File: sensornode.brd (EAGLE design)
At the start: 113 x 59.7 mm, 72 parts, among them IC1 CP2104, Q1 mmbt2222, Q2 mmbt2222, Q3 DMG3415U, SW2 KMR2, U1 TSL2591, U2 AP2112-3.3, U3 MCP73831T-2ACI/OT, U4 BMEx80, X2 ESP32_WROOM32_SKINNY, X4 20329

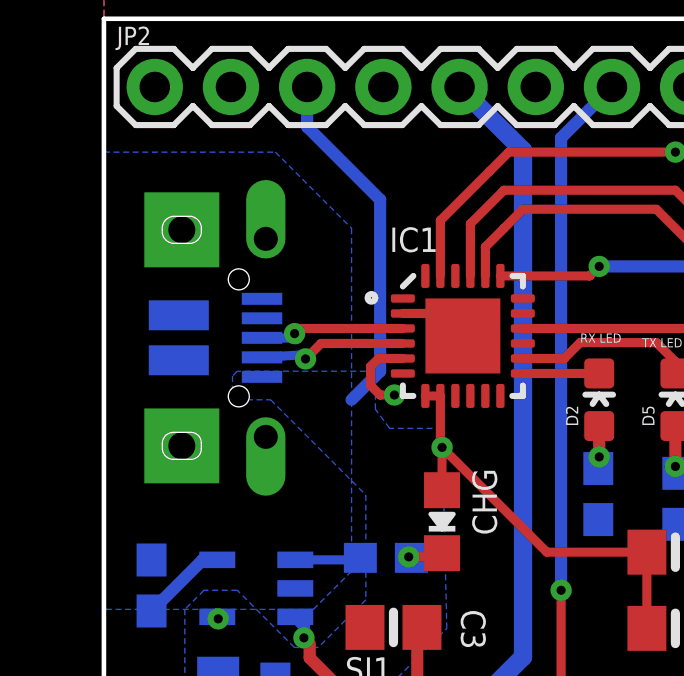
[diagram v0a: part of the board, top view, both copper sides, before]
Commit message: USB: Swapping the USB part out - twas unobtanium
the 4UCONN connector that Adafruit used is basically made of unobtanium
and more or less doesn't exist.  The part that was trying to be used
the rear prongs did not match up by any stretch of the imagination.

A mess of e-mails an annoyance ensued.

I'm swapping out the part on everything I can now, this seems to be
more common, and there's parts that are similar enough to it that
replacing it won't be a big deal.  New part is the
Amphenol FCI 10118193-0001LF
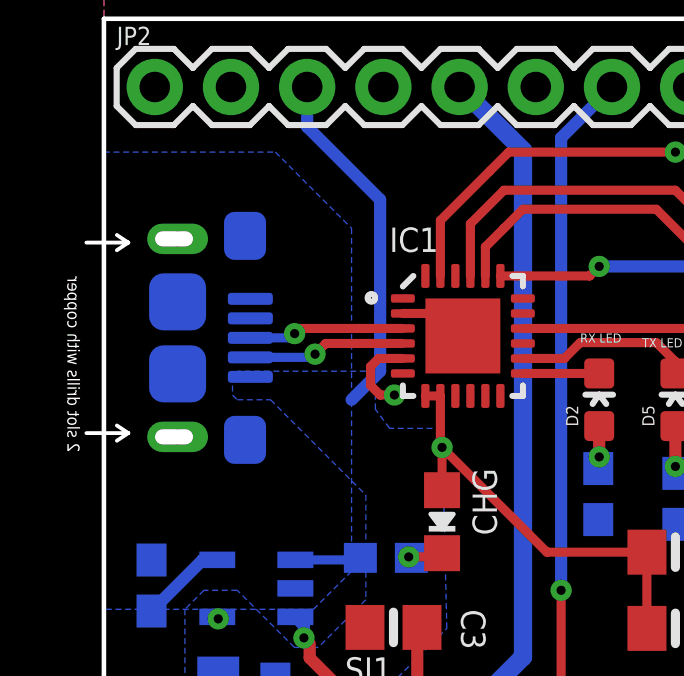
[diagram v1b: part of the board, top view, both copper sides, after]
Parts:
- X4: device microbuilder:4UCONN_20329_V2 -> microbuilder:MICRO-USB5+6P-SMD-0.65-B
- moved X4 0.63 mm to (5.13, 49.1)
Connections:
- net GND: now also X4.5, X4.S1, X4.S2, X4.S3, X4.S4, X4.S5, X4.S6; no longer X4.BASE@1, X4.BASE@2, X4.GND, X4.SPRT@1, X4.SPRT@2, X4.SPRT@3, X4.SPRT@4
- net USBD_N: now also X4.2; no longer X4.D-
- net USBD_P: now also X4.3; no longer X4.D+
- net VBUS: now also X4.1; no longer X4.VBUS
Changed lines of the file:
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@@
 <layer number="115" name="ReferenceISLANDS" color="7" fill="1" visible="yes" active="yes"/>
 <layer number="116" name="Patch_BOT" color="9" fill="4" visible="yes" active="yes"/>
+<layer number="117" name="BACKMAAT1" color="7" fill="1" visible="no" active="no"/>
 <layer number="118" name="Rect_Pads" color="7" fill="1" visible="yes" active="yes"/>
+<layer number="119" name="KAP_TEKEN" color="7" fill="1" visible="no" active="no"/>
+<layer number="120" name="KAP_MAAT1" color="7" fill="1" visible="no" active="no"/>
 <layer number="121" name="_tsilk" color="7" fill="1" visible="yes" active="yes"/>
 <layer number="122" name="_bsilk" color="7" fill="1" visible="yes" active="yes"/>
@@
 <layer number="128" name="_bValues" color="7" fill="1" visible="yes" active="yes"/>
 <layer number="129" name="Mask" color="7" fill="1" visible="yes" active="yes"/>
+<layer number="130" name="SMDSTROOK" color="7" fill="1" visible="no" active="no"/>
 <layer number="131" name="tAdjust" color="7" fill="1" visible="yes" active="yes"/>
 <layer number="132" name="bAdjust" color="7" fill="1" visible="yes" active="yes"/>
+<layer number="133" name="bottom_silk" color="7" fill="1" visible="no" active="no"/>
 <layer number="144" name="Drill_legend" color="7" fill="1" visible="yes" active="yes"/>
 <layer number="145" name="DrillLegend_01-16" color="2" fill="9" visible="yes" active="yes"/>
@@
 <attribute name="NAME" x="4.137" y="43.33875" size="0.8128" layer="26" ratio="18" rot="MR180"/>
 </element>
-<element name="X4" library="microbuilder" package="4UCONN_20329_V2" value="20329" x="4.4958" y="49.05375" rot="MR90"/>
+<element name="X4" library="microbuilder" package="MICRO-USB5+6P-SMD-0.65-B" value="20329" x="5.1308" y="49.05375" rot="MR90"/>
 <element name="JP2" library="SparkFun-Connectors" package="1X29" value="" x="1.695" y="57.41625"/>
 <element name="Q1" library="SparkFun" package="SOT23-3" value="mmbt2222" x="93.0275" y="57.15" rot="R180"/>
@@
 <contactref element="SW2" pad="A"/>
 <contactref element="SW2" pad="A'"/>
-<contactref element="X4" pad="BASE@1"/>
-<contactref element="X4" pad="BASE@2"/>
-<contactref element="X4" pad="GND"/>
-<contactref element="X4" pad="SPRT@1"/>
-<contactref element="X4" pad="SPRT@2"/>
-<contactref element="X4" pad="SPRT@3"/>
-<contactref element="X4" pad="SPRT@4"/>
+<contactref element="X4" pad="5"/>
 <contactref element="IC1" pad="2"/>
 <contactref element="IC1" pad="THERM"/>
@@
 <contactref element="C21" pad="2"/>
 <contactref element="C20" pad="2"/>
+<contactref element="X4" pad="S1"/>
+<contactref element="X4" pad="S2"/>
+<contactref element="X4" pad="S3"/>
+<contactref element="X4" pad="S4"/>
+<contactref element="X4" pad="S5"/>
+<contactref element="X4" pad="S6"/>
 <wire x1="96.995" y1="44.4275" x2="94.615" y2="43.18" width="0" layer="19" extent="1-1"/>
 </signal>
@@
 <wire x1="9.09625" y1="33.44875" x2="7.3025" y2="35.2425" width="0.4064" layer="16"/>
 <wire x1="7.3025" y1="35.2425" x2="7.3025" y2="37.465" width="0.4064" layer="16"/>
-<contactref element="X4" pad="VBUS"/>
+<contactref element="X4" pad="1"/>
 <contactref element="IC1" pad="8"/>
 <contactref element="C20" pad="1"/>
@@
 </signal>
 <signal name="USBD_P" class="1">
-<contactref element="X4" pad="D+"/>
+<contactref element="X4" pad="3"/>
 <contactref element="IC1" pad="3"/>
-<wire x1="5.2708" y1="49.05375" x2="6.419565625" y2="49.042203125" width="0.3048" layer="16"/>
 <via x="6.357075" y="49.195234375" extent="1-16" drill="0.3048"/>
-<wire x1="6.419565625" y1="49.042203125" x2="6.357075" y2="49.195234375" width="0.4064" layer="16"/>
 <wire x1="9.96484375" y1="49.367246875" x2="6.5290875" y2="49.367246875" width="0.3048" layer="1"/>
 <wire x1="6.5290875" y1="49.367246875" x2="6.357075" y2="49.195234375" width="0.3048" layer="1"/>
+<wire x1="4.8808" y1="49.05375" x2="6.215590625" y2="49.05375" width="0.3048" layer="16"/>
+<wire x1="6.215590625" y1="49.05375" x2="6.357075" y2="49.195234375" width="0.3048" layer="16"/>
 </signal>
 <signal name="USBD_N" class="1">
-<contactref element="X4" pad="D-"/>
+<contactref element="X4" pad="2"/>
 <contactref element="IC1" pad="4"/>
-<wire x1="5.2708" y1="48.40375" x2="6.65755625" y2="48.48991875" width="0.3048" layer="16"/>
-<via x="6.720215625" y="48.35099375" extent="1-16" drill="0.3048"/>
-<wire x1="6.65755625" y1="48.48991875" x2="6.720215625" y2="48.35099375" width="0.4064" layer="16"/>
-<wire x1="9.96484375" y1="48.867246875" x2="7.23646875" y2="48.867246875" width="0.3048" layer="1"/>
-<wire x1="7.23646875" y1="48.867246875" x2="6.720215625" y2="48.35099375" width="0.3048" layer="1"/>
+<via x="7.037715625" y="48.50974375" extent="1-16" drill="0.3048"/>
+<wire x1="4.8808" y1="48.40375" x2="6.931721875" y2="48.40375" width="0.3048" layer="16"/>
+<wire x1="6.931721875" y1="48.40375" x2="7.037715625" y2="48.50974375" width="0.3048" layer="16"/>
+<wire x1="9.96484375" y1="48.867246875" x2="7.39521875" y2="48.867246875" width="0.3048" layer="1"/>
+<wire x1="7.39521875" y1="48.867246875" x2="7.037715625" y2="48.50974375" width="0.3048" layer="1"/>
 </signal>
 <signal name="RTS">

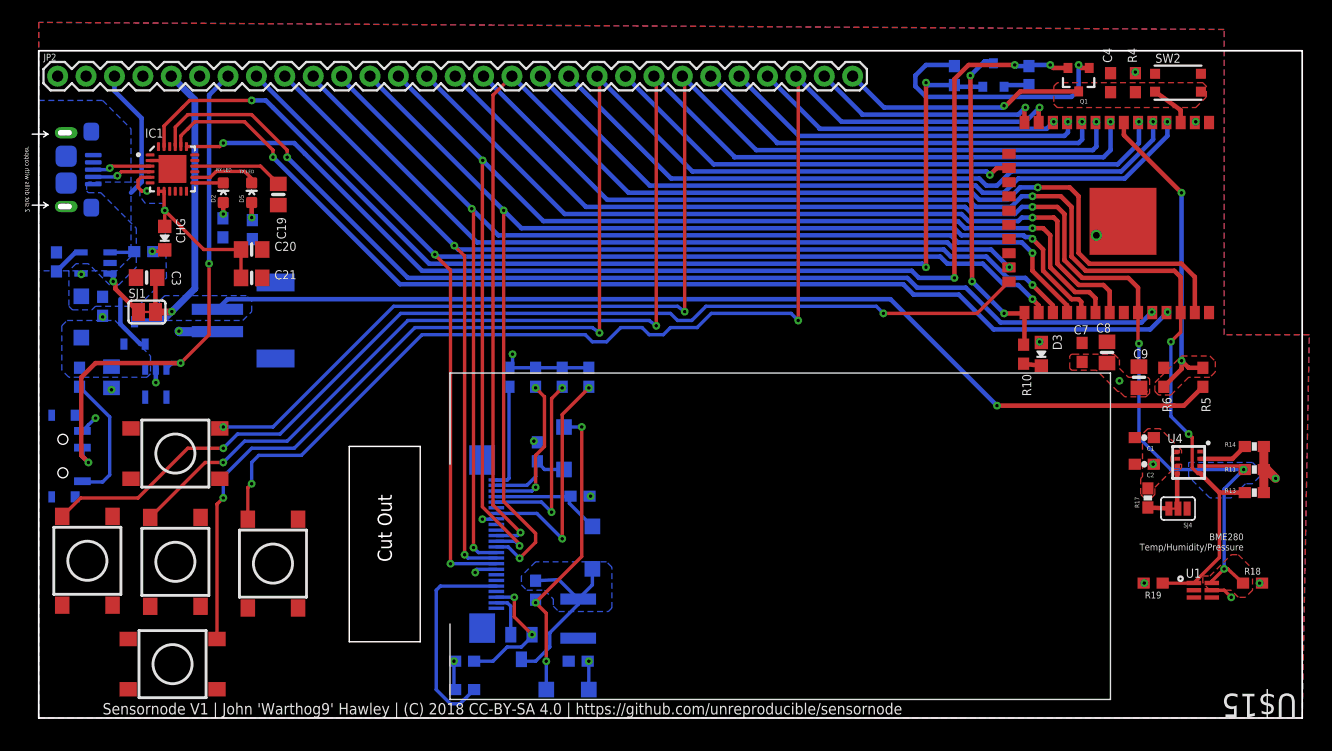
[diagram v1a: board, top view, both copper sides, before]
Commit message: Moving sensors down-making room for wifi keep out
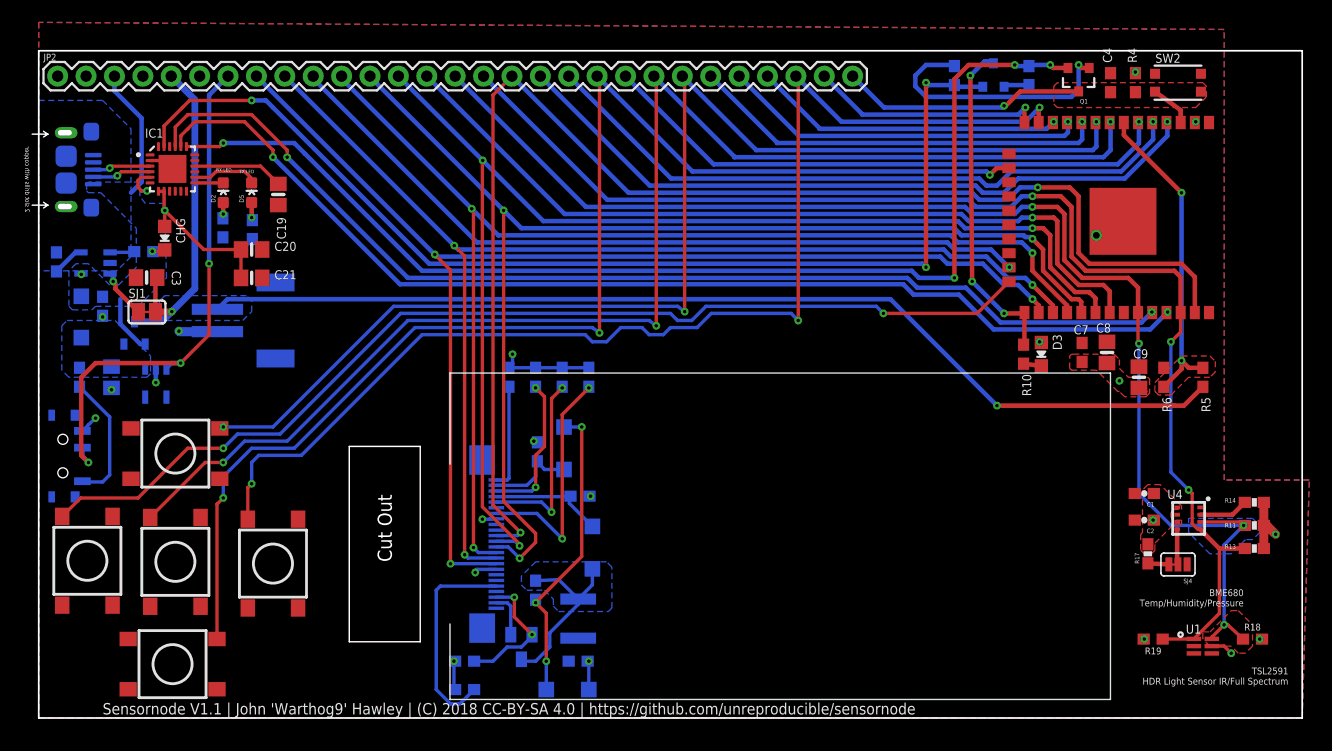
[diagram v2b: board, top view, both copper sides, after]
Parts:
- moved SJ4 5.00 mm to (101.9, 13.7)
- moved C1 5.00 mm to (98.9, 20.1)
- moved C2 5.00 mm to (98.9, 17.7)
- moved R11 5.00 mm to (108.7, 17.2)
- moved R14 5.00 mm to (108.7, 19.3)
- moved U1 5.00 mm to (104.1, 6.43)
- moved U4 5.00 mm to (102.9, 17.9)
- moved R18 5.00 mm to (108.6, 7.07)
- moved R19 5.00 mm to (99.7, 7.07)
- moved R13 5.00 mm to (108.7, 15.2)
- moved R17 5.00 mm to (99.2, 14.7)
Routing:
- net SDA: track 113.8 -> 118.8 mm
- net SCL: track 108.9 -> 113.9 mm
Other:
- board text added: "BME680 Temp/Humidity/Pressure"
- board text added: "Sensornode V1.1 | John 'Warthog9' Hawley | (C) 2018 CC-BY-SA 4.0 | https://github.com/unreproducible/sensornode"
- board text added: "TSL2591 HDR Light Sensor IR/Full Spectrum"
- board text removed: "BME280 Temp/Humidity/Pressure"
- board text removed: "Sensornode V1 | John 'Warthog9' Hawley | (C) 2018 CC-BY-SA 4.0 | https://github.com/unreproducible/sensornode"

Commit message: Clearing some space around the eink screen
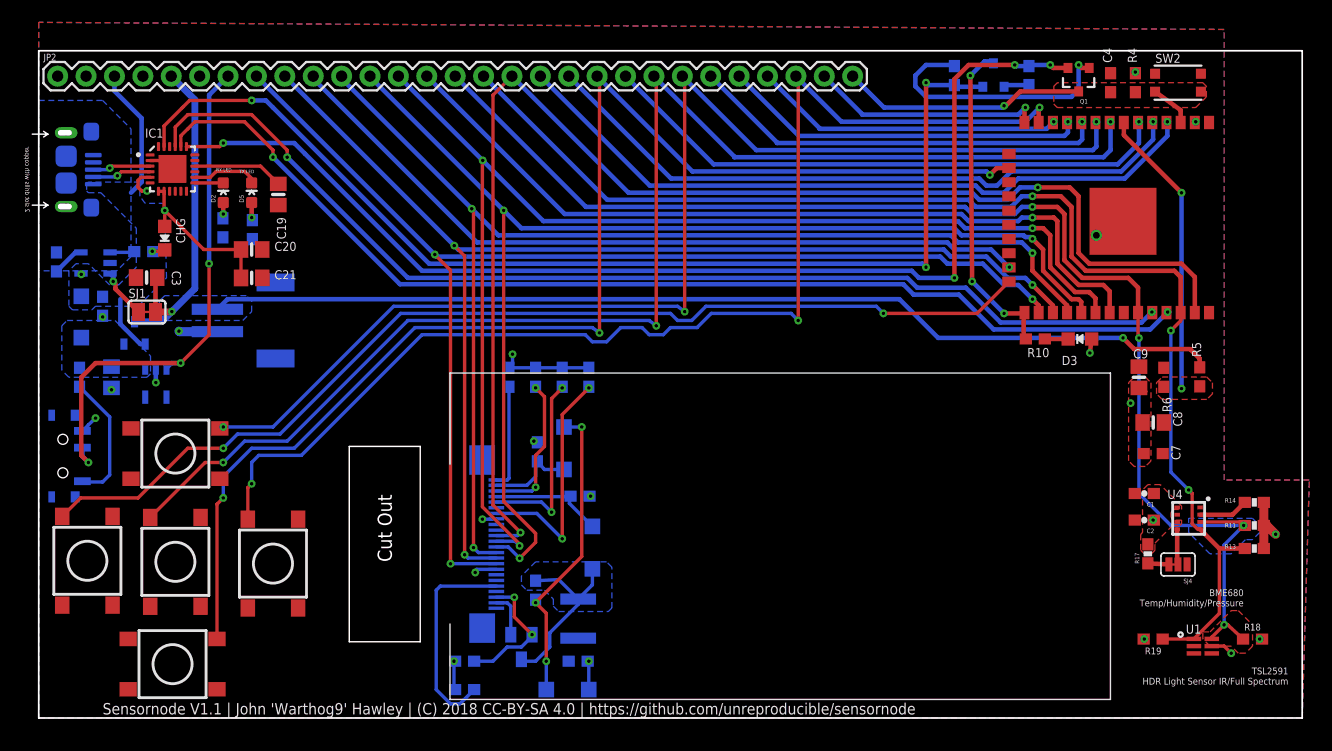
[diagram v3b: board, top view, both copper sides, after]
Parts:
- moved C7 11.1 mm to (99.7, 23.7), turned to 0 degrees
- moved C8 7.51 mm to (99.7, 26.4), turned to 0 degrees
- moved D3 3.71 mm to (93.1, 33.9), turned to 90 degrees
- moved R10 1.72 mm to (89.2, 33.9), turned to 0 degrees
- moved R5 0.28 mm to (103.9, 30.5), turned to 90 degrees
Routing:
- net A13_I35: track 28.6 -> 25.9 mm
- net VBAT: track 124.3 -> 122.3 mm
- net 3.3V: track 11.6 -> 12.7 mm
- net GPIO0: track 29.9 -> 29.3 mm

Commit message: increase board height to 61mm
Also adjust some parts near the top
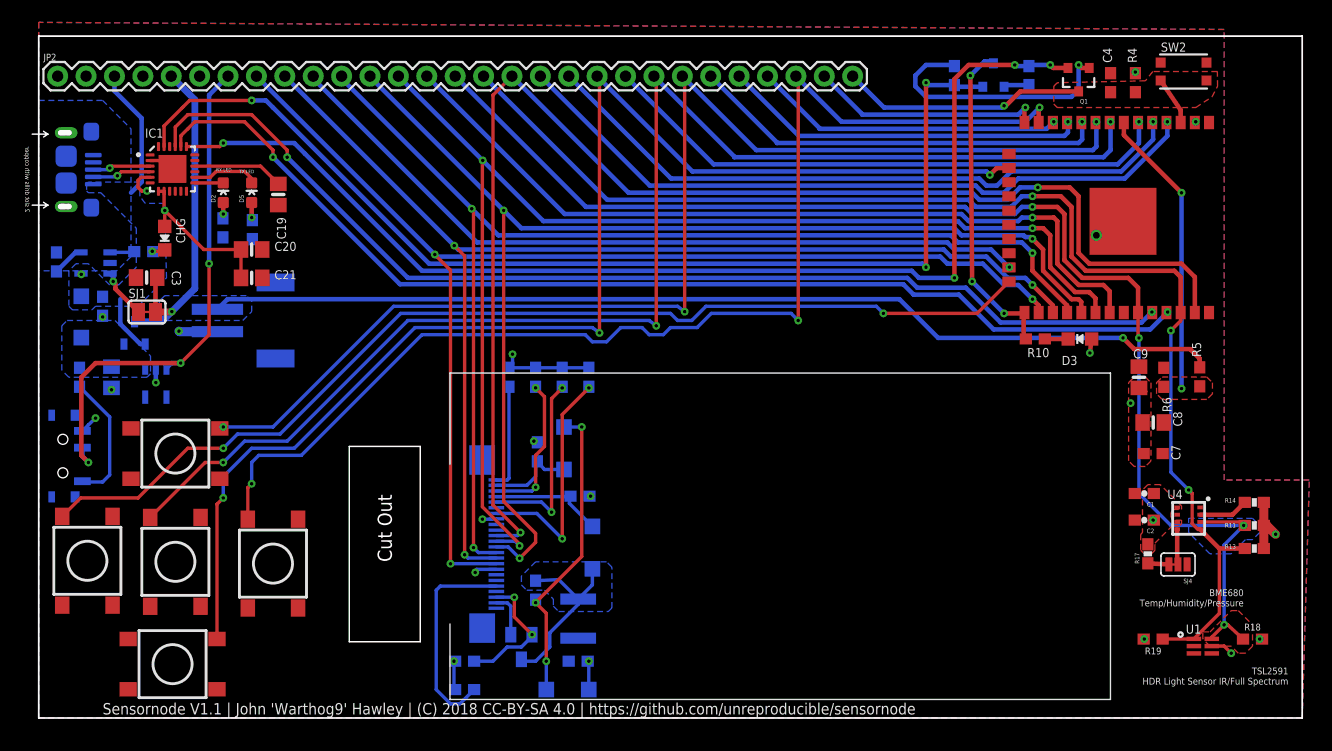
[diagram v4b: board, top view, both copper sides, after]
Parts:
- moved SW2 1.12 mm to (102.4, 57.8)
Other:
- board size 113 x 59.7 mm -> 113 x 61 mm
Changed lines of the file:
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@@
 <setting verticaltext="up"/>
 </settings>
-<grid distance="1" unitdist="mm" unit="mm" style="lines" multiple="1" display="yes" altdistance="0.5" altunitdist="mm" altunit="mm"/>
+<grid distance="1" unitdist="mm" unit="mm" style="lines" multiple="1" display="yes" altdistance="0.1" altunitdist="mm" altunit="mm"/>
 <layers>
 <layer number="1" name="Top" color="4" fill="1" visible="yes" active="yes"/>
@@
 <board>
 <plain>
-<wire x1="113.03" y1="0" x2="113.03" y2="59.69" width="0.1524" layer="20"/>
-<wire x1="113.03" y1="59.69" x2="0" y2="59.69" width="0.1524" layer="20"/>
-<wire x1="0" y1="59.69" x2="0" y2="0" width="0.1524" layer="20"/>
+<wire x1="113.03" y1="0" x2="113.03" y2="61" width="0.1524" layer="20"/>
+<wire x1="113.03" y1="61" x2="0" y2="61" width="0.1524" layer="20"/>
+<wire x1="0" y1="61" x2="0" y2="0" width="0.1524" layer="20"/>
 <wire x1="0" y1="0" x2="113.03" y2="0" width="0.1524" layer="20"/>
 <text x="17.93875" y="48.73625" size="0.3048" layer="21">TX LED</text>
@@
 </element>
 <element name="SJ1" library="microbuilder" package="SOLDERJUMPER_CLOSEDWIRE@1" value="" x="9.68375" y="36.322"/>
-<element name="SW2" library="microbuilder" package="BTN_KMR2_4.6X2.8" value="KMR2" x="101.9175" y="56.8325"/>
+<element name="SW2" library="microbuilder" package="BTN_KMR2_4.6X2.8" value="KMR2" x="102.4175" y="57.8325"/>
 <element name="U3" library="microbuilder" package="SOT23-5" value="MCP73831T-2ACI/OT" x="5.08" y="40.7035" smashed="yes" rot="MR270">
 <attribute name="NAME" x="4.137" y="43.33875" size="0.8128" layer="26" ratio="18" rot="MR180"/>
@@
 <contactref element="C4" pad="1"/>
 <contactref element="JP2" pad="29"/>
-<wire x1="99.8675" y1="56.0325" x2="102.155" y2="54.38" width="0.4064" layer="1"/>
+<wire x1="100.3675" y1="57.0325" x2="102.155" y2="54.38" width="0.4064" layer="1"/>
 <wire x1="102.155" y1="54.38" x2="102.155" y2="53.2675" width="0.4064" layer="1"/>
 <polygon width="0.4064" layer="1">
 <vertex x="91.1225" y="54.61"/>
 <vertex x="103.505" y="54.61"/>
-<vertex x="104.4575" y="55.5625"/>
-<vertex x="104.4575" y="56.515"/>
-<vertex x="104.14" y="56.8325"/>
+<vertex x="104.9575" y="55.5625"/>
+<vertex x="105.4575" y="56.515"/>
+<vertex x="105.44" y="57.8325"/>
+<vertex x="99.6675" y="57.8325"/>
+<vertex x="99" y="57"/>
 <vertex x="91.1225" y="56.8325"/>
 <vertex x="90.805" y="56.515"/>
